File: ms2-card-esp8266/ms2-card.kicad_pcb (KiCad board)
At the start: 2 copper layers, 100 x 54 mm, 64 parts, among them J1 Schaltregler, J10 MicroSD_SPI_CD, J11 Conn_01x06, J2 ESP Prog, J20 Smartcard Connector, J21 PogoPin, J22 Card Edge, J23 Conn_01x04, J30 USB_B_Micro, J31 Power Select, J32 Conn_01x03, Q1 MMBT3904, Q2 MMBT3904, Q3 MMBT5401, SW1 RESET, U1 ESP-12F, U10 W25Q128JVIM, U2 FM24C64B, U20 BL1551B, U3 BL1551B, U30 CP2102N-Axx-xQFN24, U4 BL1551B, U6 AMS1117-3.3

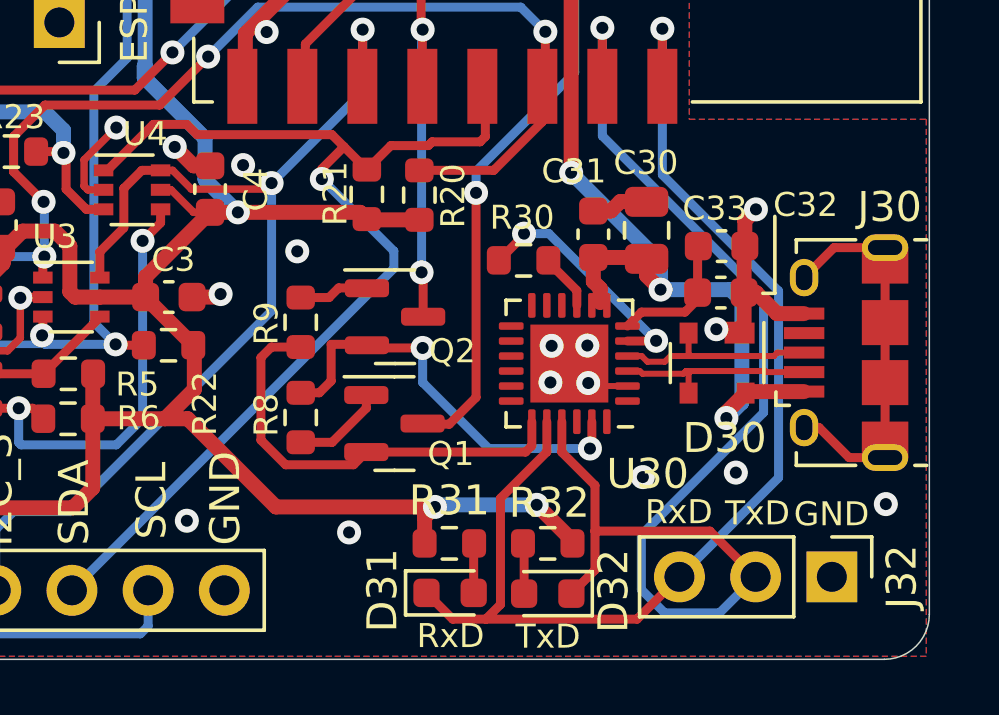
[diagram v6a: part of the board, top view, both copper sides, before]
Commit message: small changes around CP2102
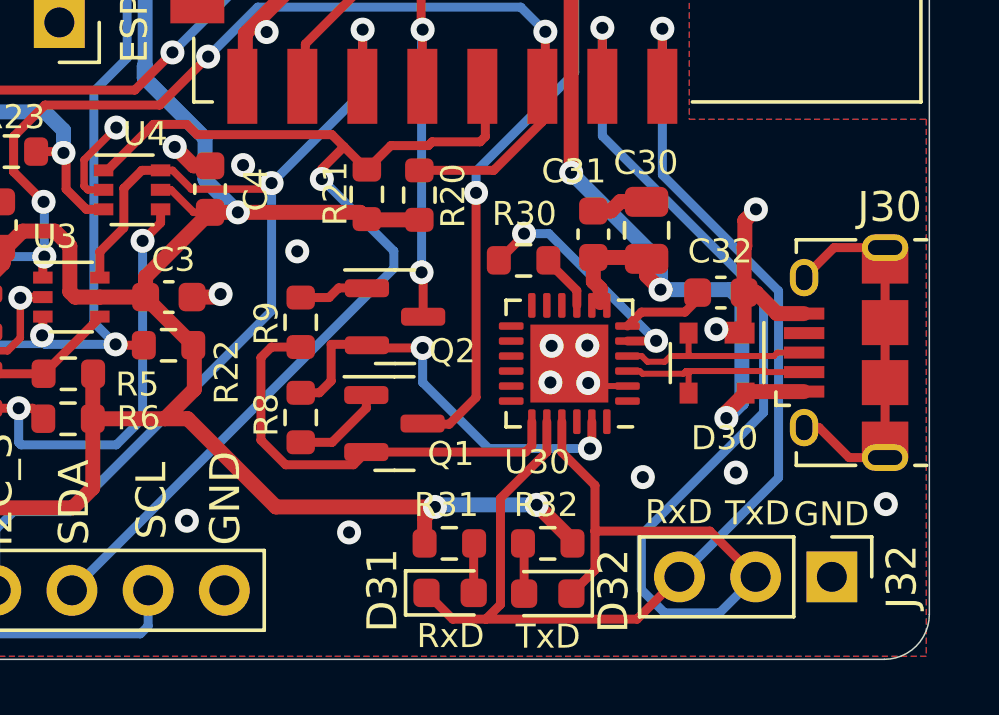
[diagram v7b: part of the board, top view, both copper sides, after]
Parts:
- removed C33: 100nF, Capacitor_SMD:C_0603_1608Metric
- C30: value 4.7uF -> 1uF
- R30: value 1k -> 4k7
- U30: value CP2102N-Axx-xQFN24 -> CP2102N-A02-GQFN24R
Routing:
- net Net-(C32-Pad1): track 4.49 -> 2.93 mm
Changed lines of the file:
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@@
     (property "Sheetname" "")
     (attr smd)
-    (fp_text reference "R32" (at -0.05 1.35) (layer "F.SilkS")
-      (effects (font (size 1 1) (thickness 0.15)))
+    (fp_text reference "R32" (at 0.055 1.285) (layer "F.SilkS")
+      (effects (font (size 0.8 0.8) (thickness 0.15)))
     )
     (fp_text value "330" (at 0 1.43) (layer "F.Fab") hide
@@
     (property "Sheetname" "")
     (attr smd)
-    (fp_text reference "C32" (at 2.825 -2.925) (layer "F.SilkS")
+    (fp_text reference "C32" (at -0.025 -1.375) (layer "F.SilkS")
       (effects (font (size 0.8 0.8) (thickness 0.15)))
     )
@@
     (descr "Capacitor SMD 0805 (2012 Metric), square (rectangular) end terminal, IPC_7351 nominal, (Body size source: IPC-SM-782 page 76, https://www.pcb-3d.com/wordpress/wp-content/uploads/ipc-sm-782a_amendment_1_and_2.pdf, https://docs.google.com/spreadsheets/d/1BsfQQcO9C6DZCsRaXUlFlo91Tg2WpOkGARC1WS5S8t0/edit?usp=sharing), generated with kicad-footprint-generator")
     (tags "capacitor")
-    (property "LCSC" "C1779")
+    (property "LCSC" "C28323")
     (property "Sheetfile" "ms2-card.kicad_sch")
     (property "Sheetname" "")
@@
       (effects (font (size 0.8 0.8) (thickness 0.15)))
     )
-    (fp_text value "4.7uF" (at 0 1.68 90) (layer "F.Fab") hide
+    (fp_text value "1uF" (at 0 1.68 90) (layer "F.Fab") hide
       (effects (font (size 1 1) (thickness 0.15)))
     )
@@
     (descr "Resistor SMD 0603 (1608 Metric), square (rectangular) end terminal, IPC_7351 nominal, (Body size source: IPC-SM-782 page 72, https://www.pcb-3d.com/wordpress/wp-content/uploads/ipc-sm-782a_amendment_1_and_2.pdf), generated with kicad-footprint-generator")
     (tags "resistor")
-    (property "LCSC" "C21190")
-    (property "Sheetfile" "ms2-card.kicad_sch")
-    (property "Sheetname" "")
-    (attr smd)
-    (fp_text reference "R30" (at -0.05 -1.425) (layer "F.SilkS")
-      (effects (font (size 0.8 0.8) (thickness 0.15)))
-    )
-    (fp_text value "1k" (at 0 1.43) (layer "F.Fab") hide
+    (property "LCSC" "C23162")
+    (property "Sheetfile" "ms2-card.kicad_sch")
+    (property "Sheetname" "")
+    (attr smd)
+    (fp_text reference "R30" (at 0.025 -1.55) (layer "F.SilkS")
+      (effects (font (size 0.8 0.8) (thickness 0.15)))
+    )
+    (fp_text value "4k7" (at 0 1.43) (layer "F.Fab") hide
       (effects (font (size 1 1) (thickness 0.15)))
     )
@@
     (property "Sheetname" "")
     (attr smd)
-    (fp_text reference "R31" (at 0 -1.43) (layer "F.SilkS")
-      (effects (font (size 1 1) (thickness 0.15)))
+    (fp_text reference "R31" (at -0.1 -1.285) (layer "F.SilkS")
+      (effects (font (size 0.8 0.8) (thickness 0.15)))
     )
     (fp_text value "330" (at 0 1.43) (layer "F.Fab") hide
@@
     (property "Sheetname" "")
     (attr smd)
-    (fp_text reference "U30" (at -2.61 -3.68) (layer "F.SilkS")
-      (effects (font (size 1 1) (thickness 0.15)))
-    )
-    (fp_text value "CP2102N-Axx-xQFN24" (at 0.5 -3.85) (layer "F.Fab") hide
+    (fp_text reference "U30" (at 1.075 -3.285) (layer "F.SilkS")
+      (effects (font (size 0.8 0.8) (thickness 0.15)))
+    )
+    (fp_text value "CP2102N-A02-GQFN24R " (at 0.5 -3.85) (layer "F.Fab") hide
       (effects (font (size 1 1) (thickness 0.15)))
     )
@@
     )
   )
-  (footprint "Capacitor_SMD:C_0603_1608Metric" (layer "F.Cu")
-    (at 191.075 140.225)
-    (descr "Capacitor SMD 0603 (1608 Metric), square (rectangular) end terminal, IPC_7351 nominal, (Body size source: IPC-SM-782 page 76, https://www.pcb-3d.com/wordpress/wp-content/uploads/ipc-sm-782a_amendment_1_and_2.pdf), generated with kicad-footprint-generator")
-    (tags "capacitor")
-    (property "LCSC" "C14663")
-    (property "Sheetfile" "ms2-card.kicad_sch")
-    (property "Sheetname" "")
-    (attr smd)
-    (fp_text reference "C33" (at -0.225 -1.25) (layer "F.SilkS")
-      (effects (font (size 0.8 0.8) (thickness 0.15)))
-    )
-    (fp_text value "100nF" (at 0 1.43) (layer "F.Fab") hide
-      (effects (font (size 1 1) (thickness 0.15)))
-    )
-    (fp_text user "${REFERENCE}" (at 0 0) (layer "F.Fab")
-      (effects (font (size 0.4 0.4) (thickness 0.06)))
-    )
-    (fp_line (start -0.14058 -0.51) (end 0.14058 -0.51) (layer "F.SilkS") (width 0.12))
-    (fp_line (start -0.14058 0.51) (end 0.14058 0.51) (layer "F.SilkS") (width 0.12))
-    (fp_line (start 1.48 -0.73) (end 1.48 0.73) (layer "F.CrtYd") (width 0.05))
-    (fp_line (start -1.48 -0.73) (end 1.48 -0.73) (layer "F.CrtYd") (width 0.05))
-    (fp_line (start -1.48 0.73) (end -1.48 -0.73) (layer "F.CrtYd") (width 0.05))
-    (fp_line (start 1.48 0.73) (end -1.48 0.73) (layer "F.CrtYd") (width 0.05))
-    (fp_line (start -0.8 -0.4) (end 0.8 -0.4) (layer "F.Fab") (width 0.1))
-    (fp_line (start -0.8 0.4) (end -0.8 -0.4) (layer "F.Fab") (width 0.1))
-    (fp_line (start 0.8 -0.4) (end 0.8 0.4) (layer "F.Fab") (width 0.1))
-    (fp_line (start 0.8 0.4) (end -0.8 0.4) (layer "F.Fab") (width 0.1))
-    (pad "1" smd roundrect (at -0.775 0) (size 0.9 0.95) (layers "F.Cu" "F.Paste" "F.Mask") (roundrect_rratio 0.25)
-      (net 48 "Net-(C32-Pad1)") (pintype "passive"))
-    (pad "2" smd roundrect (at 0.775 0) (size 0.9 0.95) (layers "F.Cu" "F.Paste" "F.Mask") (roundrect_rratio 0.25)
-      (net 2 "GND") (pintype "passive"))
-    (model "${KICAD6_3DMODEL_DIR}/Capacitor_SMD.3dshapes/C_0603_1608Metric.wrl"
-      (offset (xyz 0 0 0))
-      (scale (xyz 1 1 1))
-      (rotate (xyz 0 0 0))
-    )
-  )
   (footprint "Package_TO_SOT_SMD:SOT-223-3_TabPin2" (layer "F.Cu")
     (at 166.415 110.55)
@@
     (attr smd)
     (fp_text reference "D30" (at 2.5 -0.25 180) (layer "F.SilkS")
-      (effects (font (size 1 1) (thickness 0.15)))
+      (effects (font (size 0.8 0.8) (thickness 0.15)))
     )
     (fp_text value "SP0503BAHT" (at -0.28 2.48) (layer "F.Fab") hide
@@
     (property "Sheetname" "")
     (attr smd)
-    (fp_text reference "R22" (at -1.21 -1.945 90) (layer "F.SilkS")
+    (fp_text reference "R22" (at -1.935 -0.895 90) (layer "F.SilkS")
       (effects (font (size 0.8 0.8) (thickness 0.15)))
     )
@@
   (gr_line (start 178.93 115.94) (end 180.71 115.94) (layer "F.SilkS") (width 0.12))
   (gr_line (start 180.71 115.94) (end 180.73 116.4) (layer "F.SilkS") (width 0.12))
-  (gr_line (start 192.85 141.8) (end 192.85 139.235) (layer "F.SilkS") (width 0.12))
-  (gr_line (start 192.45 141.8) (end 192.85 141.8) (layer "F.SilkS") (width 0.12))
   (gr_line (start 155 100) (end 155 154) (layer "Dwgs.User") (width 0.15))
   (gr_arc (start 101.5 154) (mid 100.43934 153.56066) (end 100 152.5) (layer "Edge.Cuts") (width 0.05))
@@
   (segment (start 188.4025 142.425) (end 187.9375 142.89) (width 0.3) (layer "F.Cu") (net 48))
   (segment (start 190.275 142.005) (end 189.855 142.425) (width 0.3) (layer "F.Cu") (net 48))
-  (segment (start 190.275 141.775) (end 190.275 140.25) (width 0.3) (layer "F.Cu") (net 48))
   (segment (start 190.275 141.775) (end 190.275 142.005) (width 0.3) (layer "F.Cu") (net 48))
   (segment (start 189.855 142.425) (end 188.4025 142.425) (width 0.3) (layer "F.Cu") (net 48))
-  (segment (start 190.275 140.25) (end 190.3 140.225) (width 0.3) (layer "F.Cu") (net 48))
   (segment (start 175.855 103.76) (end 178.8525 103.76) (width 0.3) (layer "F.Cu") (net 49))
   (segment (start 178.8525 103.76) (end 178.8625 103.75) (width 0.3) (layer "F.Cu") (net 49))
